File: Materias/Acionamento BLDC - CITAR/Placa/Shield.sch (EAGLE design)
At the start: 37 parts, among them IC1 LMC6484, U1 DRV8811_PWP_28, U2 52207-1185

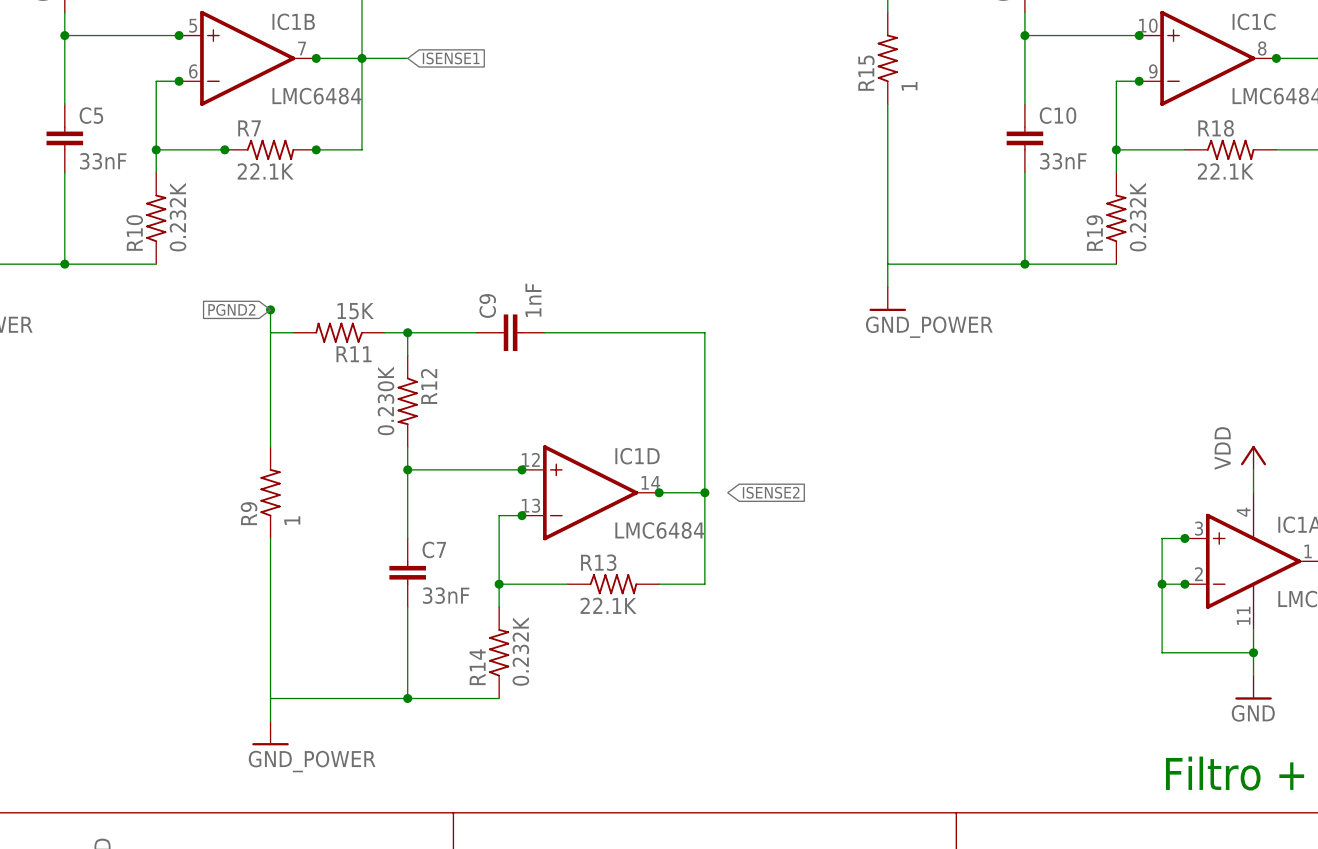
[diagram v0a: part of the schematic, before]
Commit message: adicionado BOM e PCB lucas
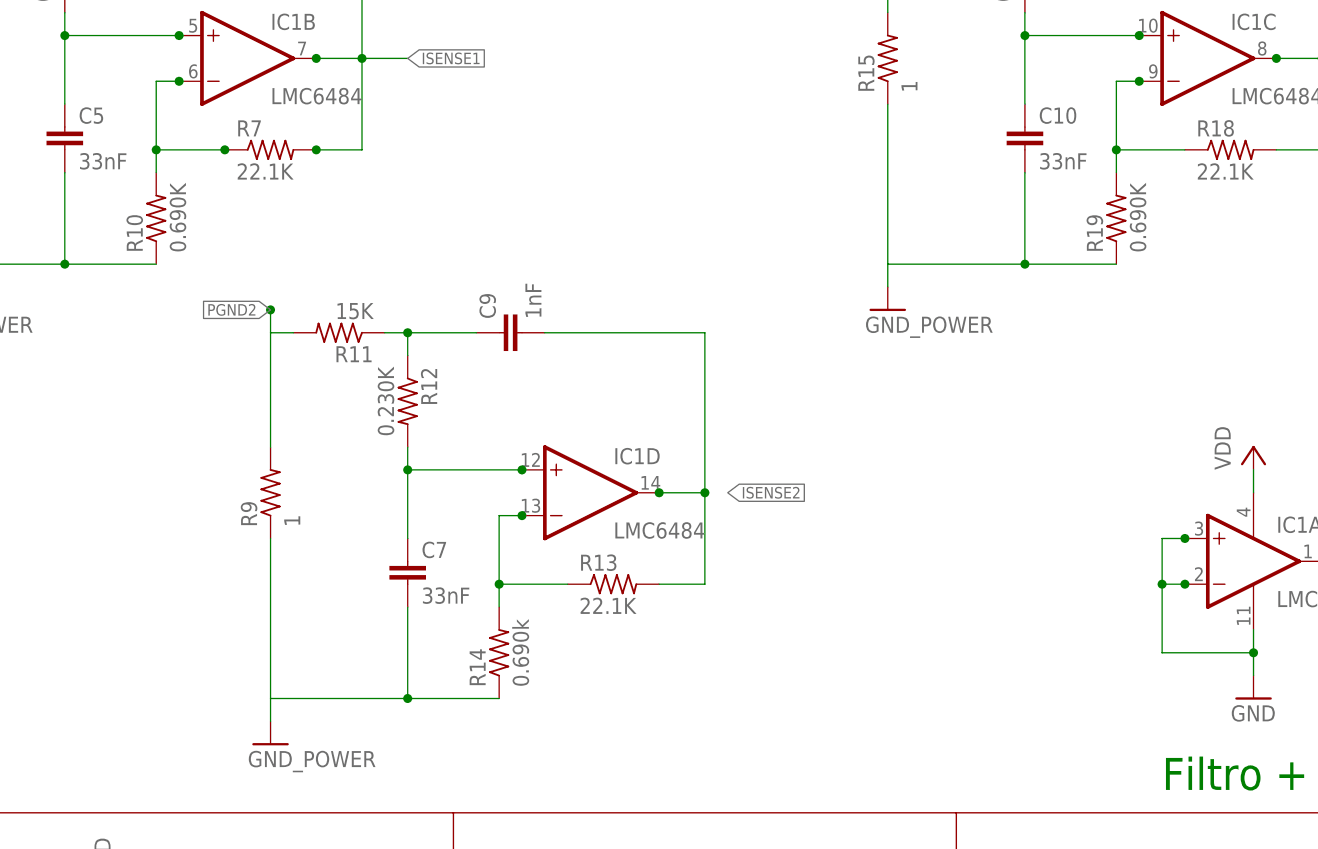
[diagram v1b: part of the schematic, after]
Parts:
- R10, R19: value 0.232K -> 0.690K
- R14: value 0.232K -> 0.690k
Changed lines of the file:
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@@
 <part name="C6" library="rcl" deviceset="C-EU" device="C1206" value="1nF"/>
 <part name="R7" library="adafruit" deviceset="R-US_" device="R1206" value="22.1K"/>
-<part name="R10" library="adafruit" deviceset="R-US_" device="R1206" value="0.232K"/>
+<part name="R10" library="adafruit" deviceset="R-US_" device="R1206" value="0.690K"/>
 <part name="R9" library="adafruit" deviceset="R-US_" device="R2512" value="1"/>
 <part name="GND4" library="supply1" deviceset="GND" device="" value="GND_POWER"/>
@@
 <part name="C9" library="rcl" deviceset="C-EU" device="C1206" value="1nF"/>
 <part name="R13" library="adafruit" deviceset="R-US_" device="R1206" value="22.1K"/>
-<part name="R14" library="adafruit" deviceset="R-US_" device="R1206" value="0.232K"/>
+<part name="R14" library="adafruit" deviceset="R-US_" device="R1206" value="0.690k"/>
 <part name="R15" library="adafruit" deviceset="R-US_" device="R2512" value="1"/>
 <part name="GND5" library="supply1" deviceset="GND" device="" value="GND_POWER"/>
@@
 <part name="C11" library="rcl" deviceset="C-EU" device="C1206" value="1nF"/>
 <part name="R18" library="adafruit" deviceset="R-US_" device="R1206" value="22.1K"/>
-<part name="R19" library="adafruit" deviceset="R-US_" device="R1206" value="0.232K"/>
+<part name="R19" library="adafruit" deviceset="R-US_" device="R1206" value="0.690K"/>
 <part name="IC1" library="lmc6484" deviceset="LMC6484" device=""/>
 <part name="GND6" library="supply1" deviceset="GND" device=""/>
